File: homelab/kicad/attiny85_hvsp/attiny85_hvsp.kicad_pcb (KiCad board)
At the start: 2 copper layers, 16 x 60 mm, 19 parts, among them J1 USB_A, Q1 2N3906, Q2 2N3904, SW1 SW_Push, U1 MIC2290

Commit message: maybe final pcb layout
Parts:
- U1: footprint Package_DFN_QFN:Micrel_MLF-8-1EP_2x2mm_P0.5mm_EP0.8x1.3mm_ThermalVias -> Package_DFN_QFN:Micrel_MLF-8-1EP_2x2mm_P0.5mm_EP0.6x1.2mm
- moved Target1 6.97 mm to (128.8, 69.3), turned to 90 degrees
- moved R3 1.60 mm to (128.8, 74.0), turned to -90 degrees
- moved R8 1.53 mm to (127.3, 77.6), turned to 180 degrees
- moved R1 1.50 mm to (130.8, 78.9), turned to 0 degrees
- moved C2 1.16 mm to (128.0, 91.1)
- moved R7 1.10 mm to (127.9, 81.6)
- moved R2 0.94 mm to (134.5, 78.9), turned to 0 degrees
- moved U1 0.88 mm to (127.4, 85.2)
- moved Q1 0.64 mm to (134.5, 76.1), turned to 90 degrees
- moved L1 0.40 mm to (133.6, 89.6), turned to 90 degrees
- moved C1 0.27 mm to (131.9, 83.9)
- moved Q2 0.18 mm to (137.9, 83.4)
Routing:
- net Net-(Master1-VCC): track 59.8 -> 74.1 mm
- net Net-(Q1-E): track 18.2 -> 30.7 mm, vias 0 -> 1
- net Net-(Master1-AREF/PB0): track 34.9 -> 43.3 mm
- net +5V: track 53.2 -> 44.8 mm, vias 2 -> 0
- net Net-(Master1-PB1): track 35.0 -> 42.2 mm
- net Net-(Q1-C): track 19.1 -> 12.3 mm
- net Net-(Master1-PB2): track 34.7 -> 40.4 mm
- net Net-(U1-SW): track 14.7 -> 11.8 mm
- net Net-(Q1-B): track 10.1 -> 7.47 mm
- net Net-(Q2-C): track 3.05 -> 4.43 mm
- net Net-(Master1-XTAL1/PB3): track 34.7 -> 33.7 mm
- net GND: track 1.87 -> 2.76 mm, vias 3 -> 1
- net Net-(U1-FB): track 8.10 -> 8.91 mm

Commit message: maybe milable hvsp pcb
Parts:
- moved R1 0.99 mm to (131.3, 78.0)
- moved Q1 0.93 mm to (134.8, 75.2)
- moved R7 0.60 mm to (128.0, 81.0)
- moved R8 0.57 mm to (127.5, 77.0)
- moved R6 0.54 mm to (127.5, 101.5)
- moved R2 0.53 mm to (134.6, 78.4)
- moved R4 0.37 mm to (138.1, 92.1)
- moved Q2 0.29 mm to (137.6, 83.5)
- moved D1 0.29 mm to (127.9, 96.9)
- moved R5 0.28 mm to (138.2, 88.6)
- moved L1 0.16 mm to (133.4, 89.6)
- turned SW1 to 0 degrees
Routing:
- net Net-(Master1-VCC): track 74.1 -> 59.7 mm
- net Net-(Q1-E): track 30.7 -> 20.5 mm, vias 1 -> 2
- net Net-(Master1-XTAL1/PB3): track 33.7 -> 29.8 mm
- net +5V: track 44.8 -> 41.9 mm
- net GND: track 2.76 -> 0.00 mm
- net Net-(Q1-C): track 12.3 -> 9.93 mm
- net Net-(Master1-PB2): track 40.4 -> 42.3 mm
- net Net-(Q2-C): track 4.43 -> 5.46 mm
- net Net-(Q1-B): track 7.47 -> 8.44 mm
- net Net-(U1-SW): track 11.8 -> 11.0 mm
- net Net-(U1-FB): track 8.91 -> 8.30 mm
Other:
- board size 16 x 60 mm -> 16.4 x 60 mm

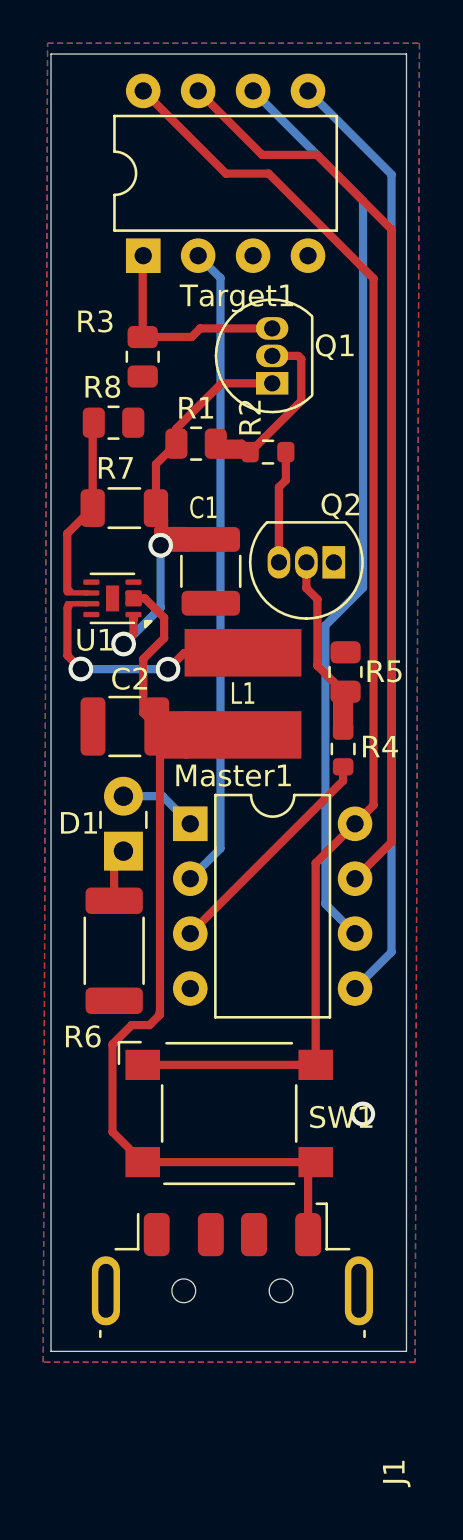
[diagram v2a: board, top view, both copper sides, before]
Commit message: removed teardrops and properly sized thermal reliefs
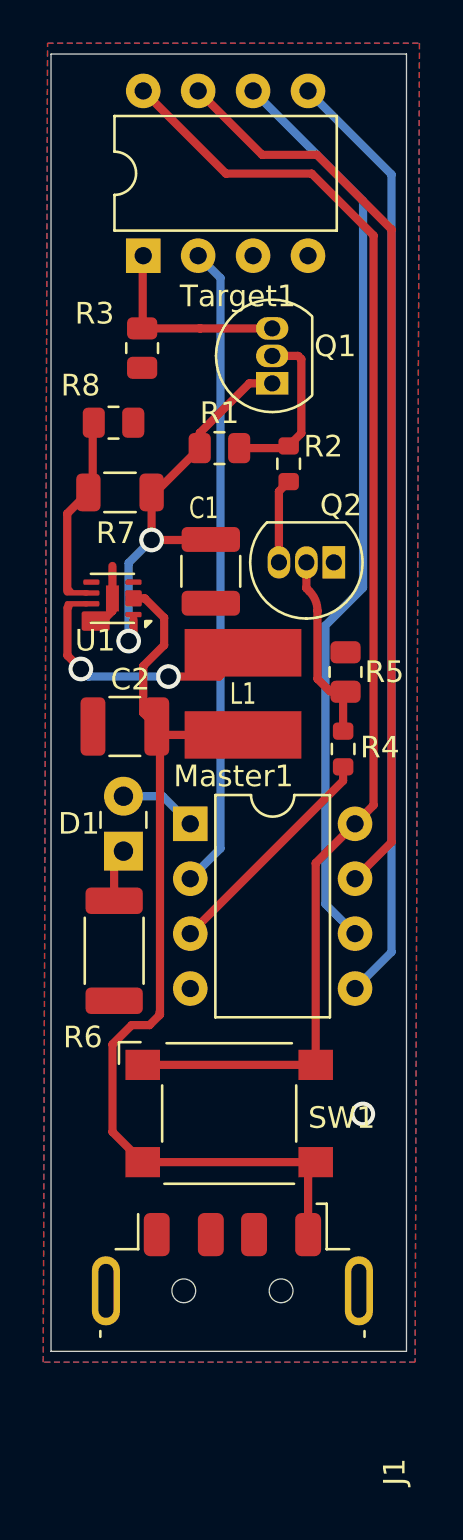
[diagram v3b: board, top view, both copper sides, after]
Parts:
- moved R1 1.10 mm to (132.3, 78.2)
- moved R2 1.10 mm to (135.6, 79.0), turned to -90 degrees
- moved R7 0.75 mm to (127.8, 80.3)
- moved R3 0.40 mm to (128.8, 73.6)
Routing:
- net +5V: track 41.9 -> 46.2 mm
- net GND: track 0.00 -> 3.28 mm
- net Net-(Q2-C): track 5.46 -> 3.92 mm
- net Net-(Q1-E): track 20.5 -> 19.2 mm
- net Net-(Master1-VCC): track 59.7 -> 60.9 mm
- net Net-(Q1-C): track 9.93 -> 9.40 mm
- net Net-(Q2-B): track 8.78 -> 8.28 mm

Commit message: maybe bantam safe layout
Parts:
- Q1, Q2: footprint Package_TO_SOT_THT:TO-92_Inline -> Package_TO_SOT_THT:TO-92L_HandSolder
- moved Q1 3.66 mm to (131.3, 74.1), turned to -90 degrees
- moved R3 2.34 mm to (127.3, 71.8), turned to 180 degrees
- moved R1 1.58 mm to (132.4, 79.8)
- moved R8 1.07 mm to (126.6, 76.4), turned to -90 degrees
- moved R2 0.92 mm to (135.9, 79.8), turned to 0 degrees
- moved Q2 0.49 mm to (137.7, 83.0)
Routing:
- net Net-(D1-A): track 3.62 -> 0.00 mm
- net Net-(Master1-XTAL1/PB3): track 29.8 -> 33.1 mm
- net Net-(Q1-C): track 9.40 -> 12.3 mm
- net Net-(U1-SW): track 11.2 -> 8.48 mm
- net Net-(Q1-E): track 19.2 -> 21.1 mm
- net GND: track 3.28 -> 5.00 mm, vias 1 -> 2
- net Net-(Q1-B): track 8.00 -> 8.73 mm

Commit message: bantam friendly layout
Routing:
- net GND: track 5.00 -> 119.9 mm, vias 2 -> 1
- net Net-(U1-SW): track 8.48 -> 12.4 mm
- net Net-(Master1-XTAL1/PB3): track 33.1 -> 31.1 mm
- net Net-(Q2-C): track 3.94 -> 5.76 mm
- net +5V: track 45.7 -> 46.7 mm
- net Net-(Q1-E): track 21.1 -> 22.0 mm
- net Net-(Q1-C): track 12.3 -> 13.1 mm
- removed copper zone on B.Cu, net GND
- removed copper zone on F.Cu, net GND
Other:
- board size 16.4 x 60 mm -> 16.9 x 60 mm
